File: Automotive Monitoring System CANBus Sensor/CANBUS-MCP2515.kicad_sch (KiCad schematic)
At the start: 7 parts, among them U4 MCP2515-xSO, Y2 16MHz

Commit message: ok updated the footprints. now toi get the DRC and a then PCB layout
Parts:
- C4, C5, C6, C7: footprint (none) -> Capacitor_SMD:C_1206_3216Metric_Pad1.33x1.80mm_HandSolder
- R5: footprint (none) -> Resistor_THT:R_Axial_DIN0207_L6.3mm_D2.5mm_P2.54mm_Vertical
- Y2: footprint (none) -> Crystal:Crystal_HC49-U_Vertical
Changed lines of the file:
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@@
 			)
 		)
-		(property "Footprint" ""
+		(property "Footprint" "Capacitor_SMD:C_1206_3216Metric_Pad1.33x1.80mm_HandSolder"
 			(at 97.4852 44.45 0)
 			(effects
@@
 			)
 		)
-		(property "Footprint" ""
+		(property "Footprint" "Resistor_THT:R_Axial_DIN0207_L6.3mm_D2.5mm_P2.54mm_Vertical"
 			(at 162.56 95.758 90)
 			(effects
@@
 			)
 		)
-		(property "Footprint" ""
+		(property "Footprint" "Crystal:Crystal_HC49-U_Vertical"
 			(at 81.28 90.17 0)
 			(effects
@@
 			)
 		)
-		(property "Footprint" ""
+		(property "Footprint" "Capacitor_SMD:C_1206_3216Metric_Pad1.33x1.80mm_HandSolder"
 			(at 64.77 82.8548 0)
 			(effects
@@
 			)
 		)
-		(property "Footprint" ""
+		(property "Footprint" "Capacitor_SMD:C_1206_3216Metric_Pad1.33x1.80mm_HandSolder"
 			(at 110.1852 44.45 0)
 			(effects
@@
 			)
 		)
-		(property "Footprint" ""
+		(property "Footprint" "Capacitor_SMD:C_1206_3216Metric_Pad1.33x1.80mm_HandSolder"
 			(at 64.77 95.5548 0)
 			(effects

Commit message: tweaked footprints and made a bunch SMD for space saving. getting the board mostly placed before routing.
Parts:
- R5: footprint Resistor_THT:R_Axial_DIN0207_L6.3mm_D2.5mm_P2.54mm_Vertical -> Resistor_SMD:R_1206_3216Metric_Pad1.30x1.75mm_HandSolder
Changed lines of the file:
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@@
 			)
 		)
-		(property "Footprint" "Resistor_THT:R_Axial_DIN0207_L6.3mm_D2.5mm_P2.54mm_Vertical"
+		(property "Footprint" "Resistor_SMD:R_1206_3216Metric_Pad1.30x1.75mm_HandSolder"
 			(at 162.56 95.758 90)
 			(effects

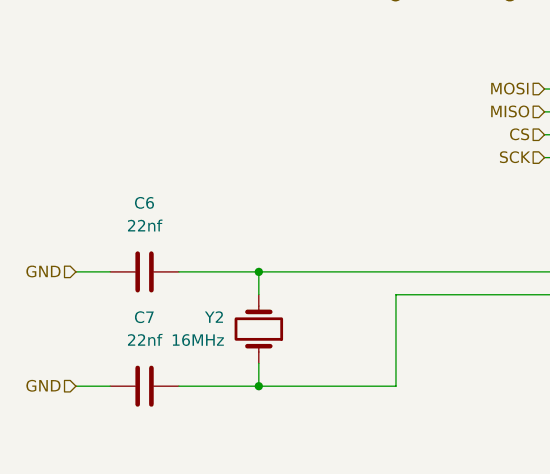
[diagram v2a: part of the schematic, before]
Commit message: ammending my last commit to have the correct cap values of 22pF
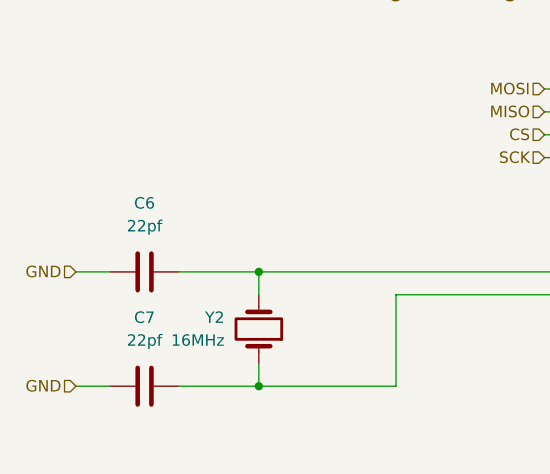
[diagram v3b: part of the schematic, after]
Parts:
- C6, C7: value 22nf -> 22pf
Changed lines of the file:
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@@
 			)
 		)
-		(property "Value" "22nf"
+		(property "Value" "22pf"
 			(at 68.58 78.74 90)
 			(effects
@@
 			)
 		)
-		(property "Value" "22nf"
+		(property "Value" "22pf"
 			(at 68.58 91.44 90)
 			(effects
